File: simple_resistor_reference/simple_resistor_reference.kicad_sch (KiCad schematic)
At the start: 1 part

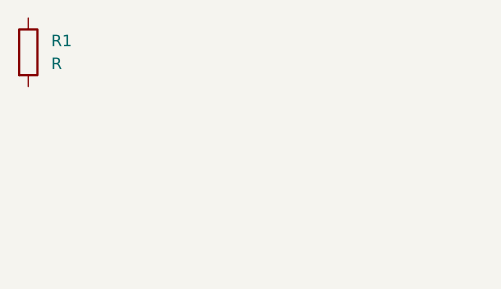
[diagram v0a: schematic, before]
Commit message: adding updated testing code
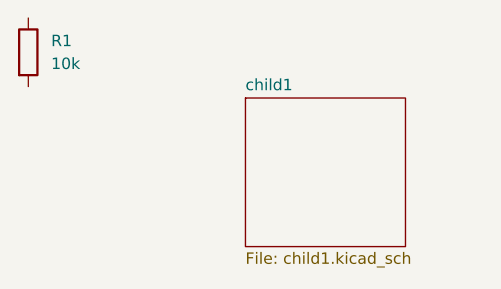
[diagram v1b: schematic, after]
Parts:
- R1: value R -> 10k; footprint (none) -> Resistor_SMD:R_0603_1608Metric
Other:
- added sheet child1 (child1.kicad_sch)
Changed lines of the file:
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@@
 			)
 		)
-		(property "Value" "R"
+		(property "Value" "10k"
 			(at 128.27 82.5499 0)
 			(effects
@@
 			)
 		)
-		(property "Footprint" ""
+		(property "Footprint" "Resistor_SMD:R_0603_1608Metric"
 			(at 123.952 81.28 90)
 			(effects
@@
 				)
 			)
+		)
+	)
+	(sheet
+		(at 149.86 86.36)
+		(size 17.78 16.51)
+		(exclude_from_sim no)
+		(in_bom yes)
+		(on_board yes)
+		(dnp no)
+		(fields_autoplaced yes)
+		(stroke
+			(width 0.1524)
+			(type solid)
+		)
+		(fill
+			(color 0 0 0 0.0000)
+		)
+		(property "Sheetname" "child1"
+			(at 149.86 85.6484 0)
+			(effects
+				(font
+					(size 1.27 1.27)
+				)
+				(justify left bottom)
+			)
+		)
+		(property "Sheetfile" "child1.kicad_sch"
+			(at 149.86 103.4546 0)
+			(effects
+				(font
+					(size 1.27 1.27)
+				)
+				(justify left top)
+			)
+		)
+		(instances
+			(project "simple_resistor_reference"
+				(path "/8ea40386-79fd-4dea-8cc4-e20a6a247364"
+					(page "2")
+				)
+			)
